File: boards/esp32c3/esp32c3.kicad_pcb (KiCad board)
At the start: 2 copper layers, 32 x 49 mm, 26 parts, among them J1 USB-C, J2 IO, Q1 AO3401A, SW1 RESET, SW2 BOOT, U1 ESP32-C3-WROOM-02-N4, U2 LP38693MP-3.3

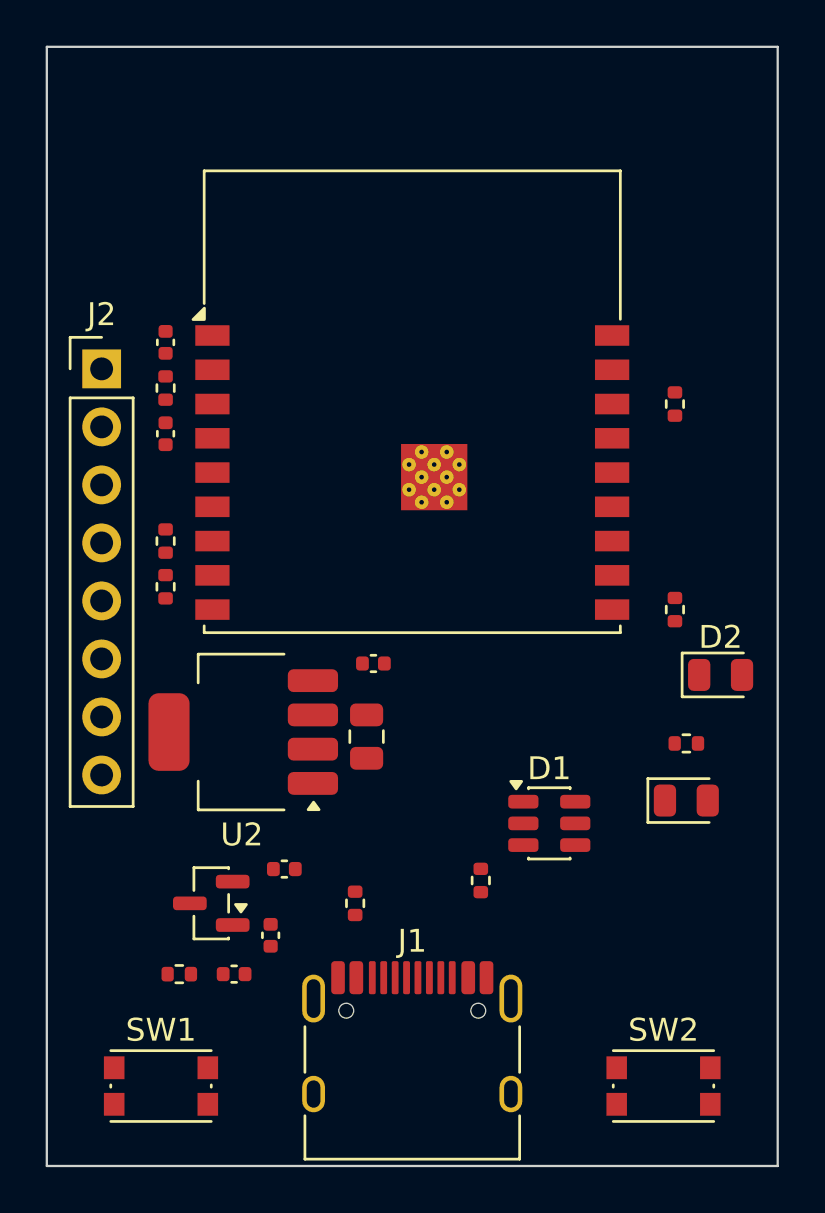
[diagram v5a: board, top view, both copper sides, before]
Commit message: build: reproducible output (seeded UUIDs, single-thread freerouting, no retry)
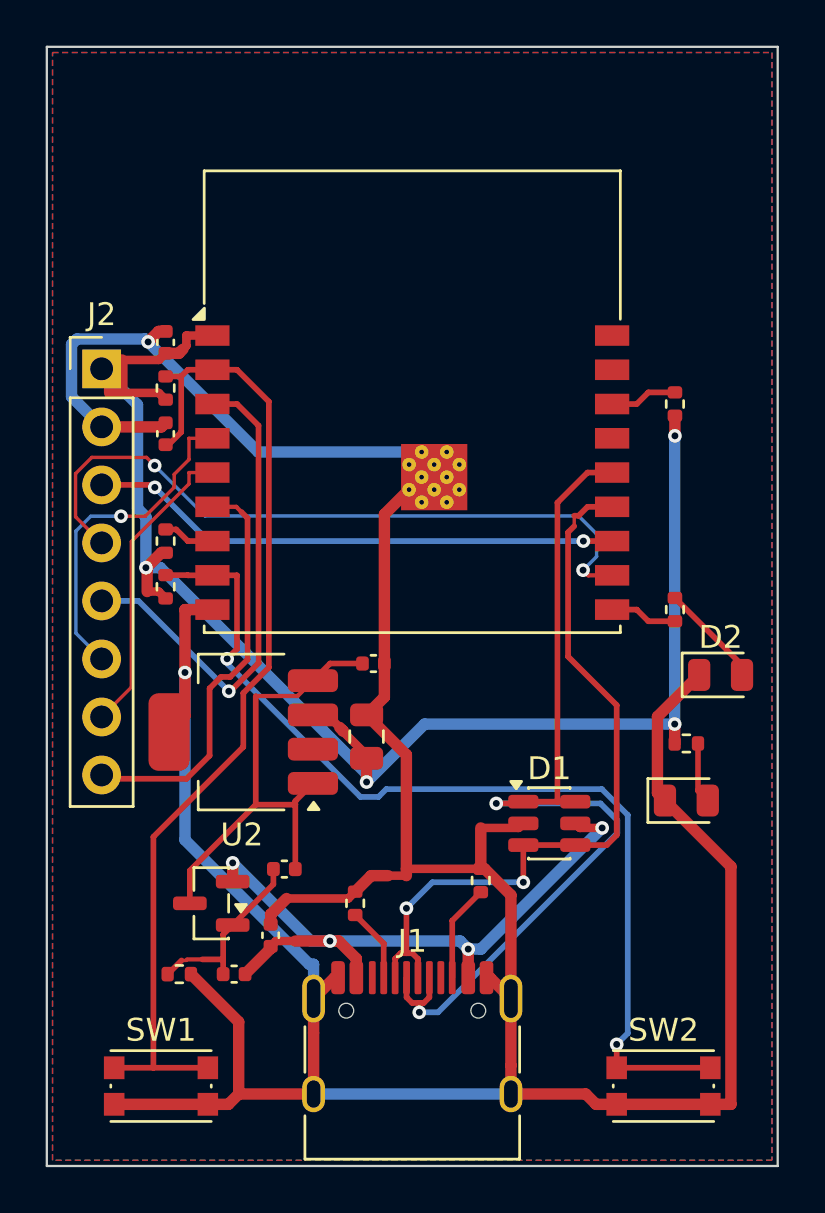
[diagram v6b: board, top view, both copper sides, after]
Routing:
- net GND: track 0.00 -> 162.3 mm, vias 0 -> 2
- net +3V3: track 0.00 -> 69.5 mm, vias 0 -> 4
- net EN: track 0.00 -> 43.9 mm
- net IO9: track 0.00 -> 43.1 mm, vias 0 -> 2
- net USB_DP: track 0.00 -> 40.9 mm, vias 0 -> 2
- net USB_DN: track 0.00 -> 33.1 mm, vias 0 -> 2
- net RXD: track 0.00 -> 31.2 mm, vias 0 -> 2
- net VBUS: track 0.00 -> 30.0 mm, vias 0 -> 4
- net TXD: track 0.00 -> 23.4 mm, vias 0 -> 2
- net IO4: track 0.00 -> 21.8 mm, vias 0 -> 1
- net VSW: track 0.00 -> 21.3 mm
- net IO7: track 0.00 -> 18.3 mm
- net IO5: track 0.00 -> 14.6 mm, vias 0 -> 1
- net IO6: track 0.00 -> 13.3 mm
- net SS_G: track 0.00 -> 8.21 mm
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- added copper zone on B.Cu, net GND
- added copper zone on F.Cu, net GND

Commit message: pcbgen: UUIDs derived from the design so routing is the same on every KiCad 10.0.x (#11)
KIID.SeedGenerator alone is not enough: KiCad 10.0.6 and 10.0.7 consume a
different number of UUIDs while loading footprints, the Specctra exporter
orders by UUID, and freerouting gave 6 vias locally vs 9 on CI.
stable_uuids() sets every item to uuid5(board/ref/kind/index) before each
save that feeds routing. esp32c3: C4 moved 0.66 mm and turned 270 deg; EN
did not route in the new order.
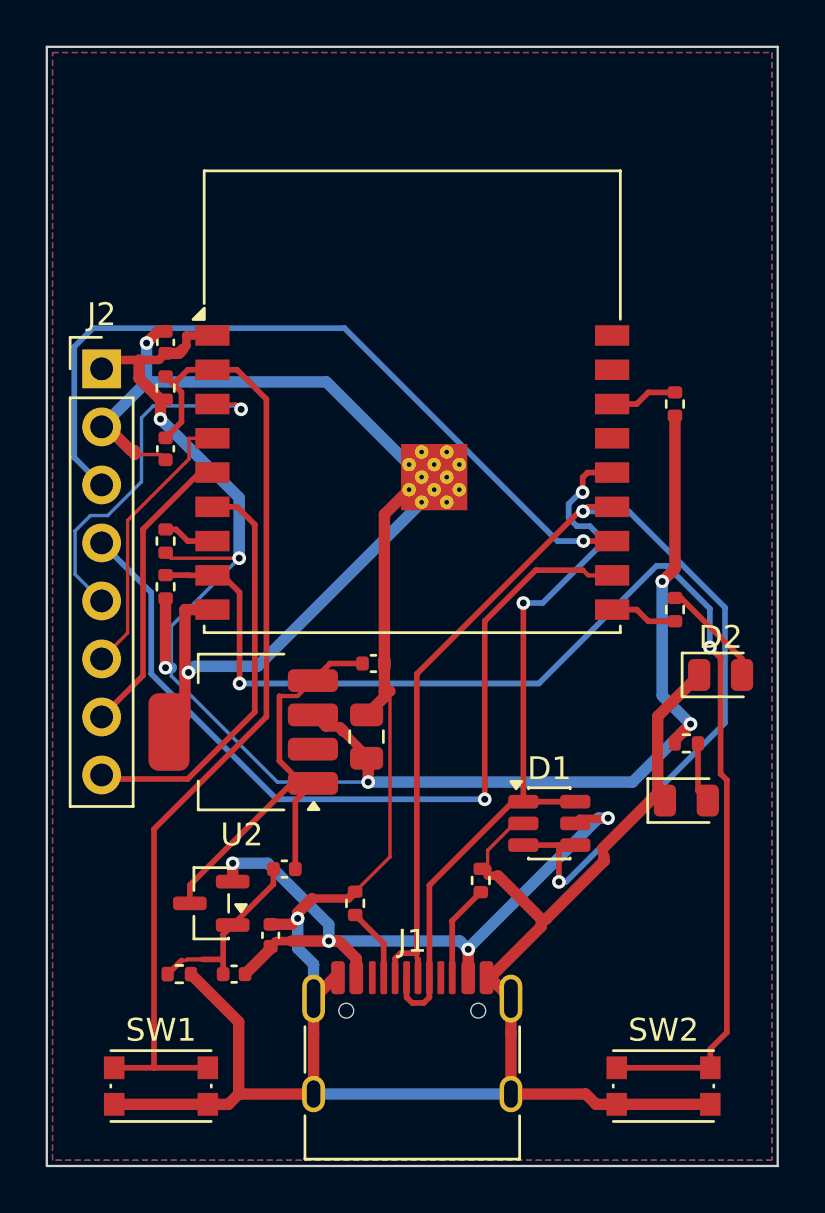
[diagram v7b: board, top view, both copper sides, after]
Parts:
- moved C4 0.66 mm to (105.2, 117.6), turned to -90 degrees
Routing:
- net USB_DN: track 33.1 -> 53.8 mm
- net GND: track 162.3 -> 147.8 mm, vias 2 -> 3
- net IO9: track 43.1 -> 55.8 mm
- net TXD: track 23.4 -> 34.3 mm, vias 2 -> 1
- net USB_DP: track 40.9 -> 33.5 mm
- net RXD: track 31.2 -> 37.9 mm, vias 2 -> 1
- net IO4: track 21.8 -> 16.1 mm
- net +3V3: track 69.5 -> 74.9 mm, vias 4 -> 6
- net IO5: track 14.6 -> 12.3 mm, vias 1 -> 0
- net VBUS: track 30.0 -> 31.1 mm
- net VSW: track 21.3 -> 20.3 mm
